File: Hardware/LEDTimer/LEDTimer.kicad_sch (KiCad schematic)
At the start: 37 parts, among them J2 LED, J3 PWR, Q1 S8050, SW1 SW_Push, SW2 SW_Push, SW3 SW_Push, SW4 SW_PWR, U1 AP7383-36WW7, U2 PIC16F1825, U3 Display_128x64_096_I2C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

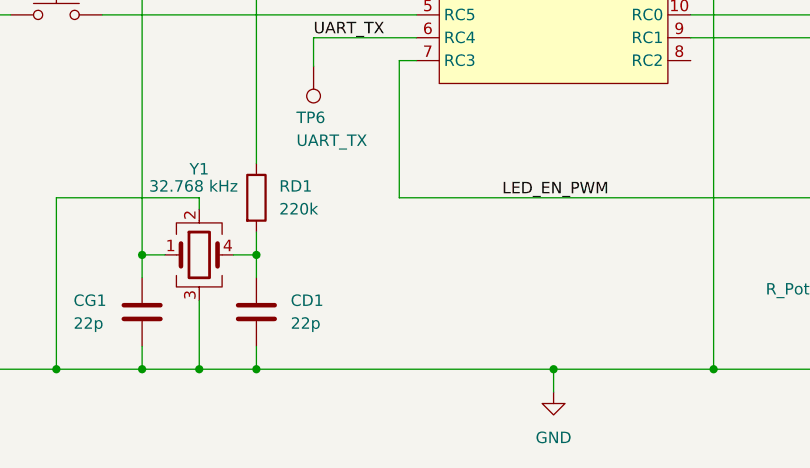
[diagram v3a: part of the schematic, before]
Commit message: PCB: add pull-down resistor to LED_EN_PWM
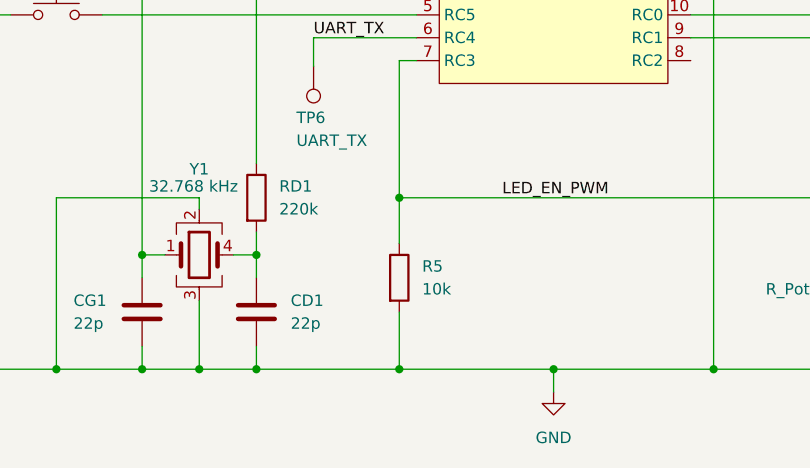
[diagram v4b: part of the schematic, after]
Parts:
- added R5: 10k, Resistor_SMD:R_0805_2012Metric_Pad1.20x1.40mm_HandSolder, symbol Device:R
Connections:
- net GND: now also R5.2
- net LED_EN_PWM: now also R5.1
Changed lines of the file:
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@@
   (junction (at 93.98 151.13) (diameter 0) (color 0 0 0 0)
   )
+  (junction (at 132.08 151.13) (diameter 0) (color 0 0 0 0)
+  )
   (junction (at 187.325 76.835) (diameter 0) (color 0 0 0 0)
   )
@@
   (junction (at 194.31 135.89) (diameter 0) (color 0 0 0 0)
   )
+  (junction (at 132.08 132.08) (diameter 0) (color 0 0 0 0)
+  )
   (junction (at 96.52 54.61) (diameter 0) (color 0 0 0 0)
   )
@@
     (stroke (width 0) (type default) (color 0 0 0 0))
   )
-  (wire (pts (xy 116.205 151.13) (xy 149.225 151.13))
+  (wire (pts (xy 116.205 151.13) (xy 132.08 151.13))
     (stroke (width 0) (type default) (color 0 0 0 0))
   )
@@
     (stroke (width 0) (type default) (color 0 0 0 0))
   )
+  (wire (pts (xy 132.08 151.13) (xy 149.225 151.13))
+    (stroke (width 0) (type default) (color 0 0 0 0))
+  )
   (wire (pts (xy 92.71 39.37) (xy 92.71 36.83))
     (stroke (width 0) (type default) (color 0 0 0 0))
@@
     (stroke (width 0) (type default) (color 0 0 0 0))
   )
+  (wire (pts (xy 132.08 132.08) (xy 132.08 137.16))
+    (stroke (width 0) (type default) (color 0 0 0 0))
+  )
   (wire (pts (xy 187.325 76.835) (xy 189.865 76.835))
     (stroke (width 0) (type default) (color 0 0 0 0))
@@
   )
   (wire (pts (xy 86.995 111.76) (xy 86.995 151.13))
+    (stroke (width 0) (type default) (color 0 0 0 0))
+  )
+  (wire (pts (xy 132.08 144.78) (xy 132.08 151.13))
     (stroke (width 0) (type default) (color 0 0 0 0))
   )
@@
     )
     (pin "1")
+  )
+  (symbol (lib_id "Device:R") (at 132.08 140.97 0) (unit 1)
+    (in_bom yes) (on_board yes) (fields_autoplaced)
+    (property "Reference" "R5" (id 0) (at 134.62 139.6999 0)
+      (effects (font (size 1.27 1.27)) (justify left))
+    )
+    (property "Value" "10k" (id 1) (at 134.62 142.2399 0)
+      (effects (font (size 1.27 1.27)) (justify left))
+    )
+    (property "Footprint" "Resistor_SMD:R_0805_2012Metric_Pad1.20x1.40mm_HandSolder" (id 2) (at 130.302 140.97 90)
+      (effects (font (size 1.27 1.27)) hide)
+    )
+    (property "Datasheet" "~" (id 3) (at 132.08 140.97 0)
+      (effects (font (size 1.27 1.27)) hide)
+    )
+    (pin "1")
+    (pin "2")
   )
   (symbol (lib_id "power:+3V3") (at 146.05 36.83 0) (unit 1)
@@
       (reference "R4") (unit 1) (value "4k7") (footprint "Resistor_SMD:R_0805_2012Metric_Pad1.20x1.40mm_HandSolder")
     )
+    (path "/258a48e0-7198-45c4-99e2-dc4beb3791d9"
+      (reference "R5") (unit 1) (value "10k") (footprint "Resistor_SMD:R_0805_2012Metric_Pad1.20x1.40mm_HandSolder")
+    )
     (path "/94034e64-17d7-4c11-8df7-c281c016c2b8"

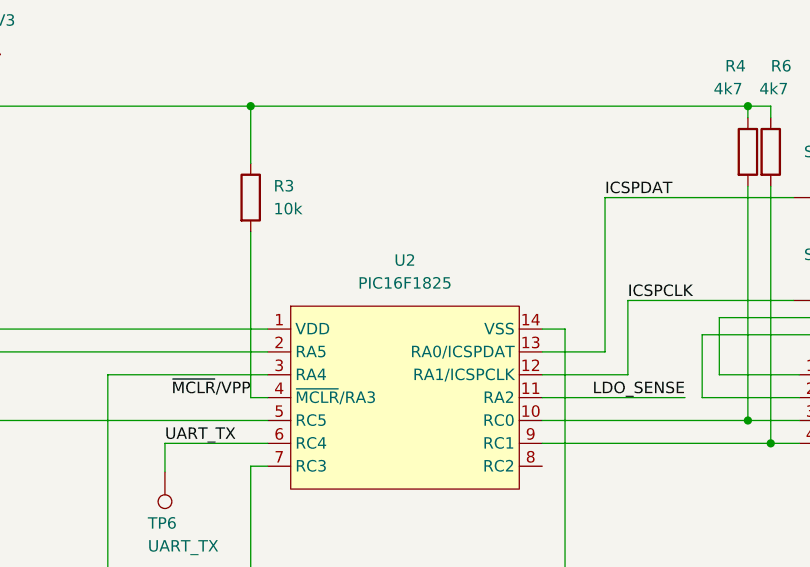
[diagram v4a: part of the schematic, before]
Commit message: PCB: swap the MCU to 16F18326
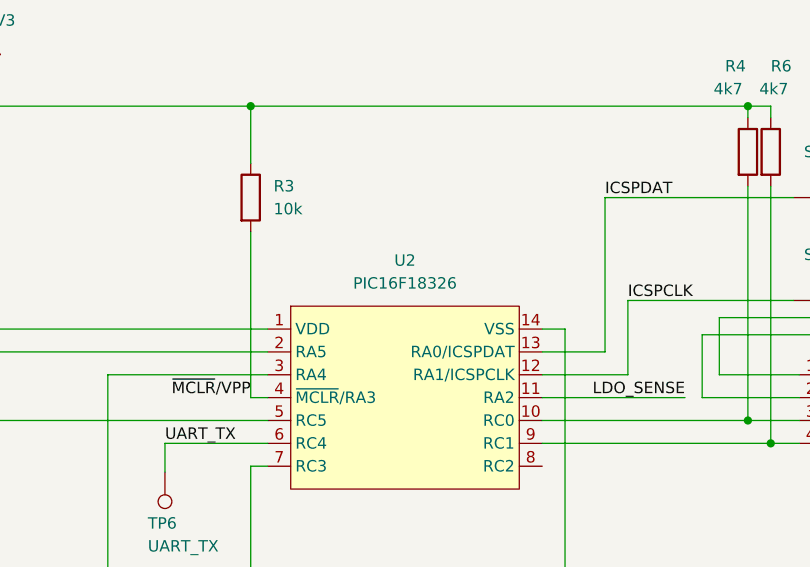
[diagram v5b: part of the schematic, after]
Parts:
- U2: value PIC16F1825 -> PIC16F18326
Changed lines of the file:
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@@
     (in_bom yes) (on_board yes) (fields_autoplaced)
     (property "Reference" "U2" (id 0) (at 149.225 93.98 0))
-    (property "Value" "PIC16F1825" (id 1) (at 149.225 96.52 0))
+    (property "Value" "PIC16F18326" (id 1) (at 149.225 96.52 0))
     (property "Footprint" "Package_SO:SOIC-14_3.9x8.7mm_P1.27mm" (id 2) (at 150.495 120.65 0)
       (effects (font (size 1.27 1.27)) hide)
     )
-    (property "Datasheet" "http://ww1.microchip.com/downloads/en/devicedoc/41440a.pdf" (id 3) (at 150.495 123.19 0)
+    (property "Datasheet" "http://ww1.microchip.com/downloads/en/devicedoc/40001839b.pdf" (id 3) (at 150.495 123.19 0)
       (effects (font (size 1.27 1.27)) hide)
     )
@@
     )
     (path "/c2cb0ccd-2078-4e7c-97f9-6201b7726a1c"
-      (reference "U2") (unit 1) (value "PIC16F1825") (footprint "Package_SO:SOIC-14_3.9x8.7mm_P1.27mm")
+      (reference "U2") (unit 1) (value "PIC16F18326") (footprint "Package_SO:SOIC-14_3.9x8.7mm_P1.27mm")
     )
     (path "/0f86b760-eddb-4ded-9e00-18319adfd610"
